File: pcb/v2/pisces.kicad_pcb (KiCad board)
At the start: 2 copper layers, 137.8 x 60.1 mm, 61 parts, among them J1 USB_B_Micro, J2 AudioJack4, SW1 SW_PUSH, SW10 SW_PUSH, SW11 SW_PUSH, SW12 SW_PUSH, SW13 SW_PUSH, SW14 SW_PUSH, SW15 SW_PUSH, SW16 SW_PUSH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

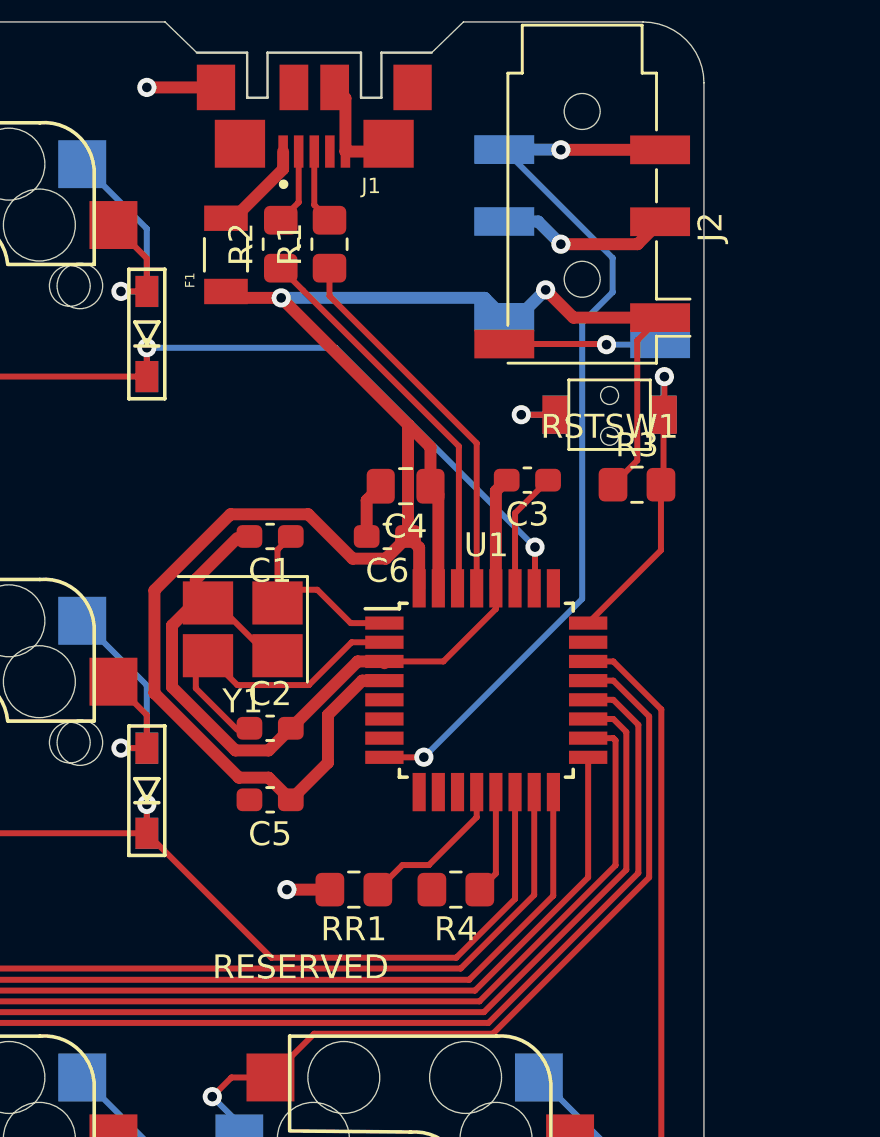
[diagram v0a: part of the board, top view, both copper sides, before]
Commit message: pisces V2.1 option 2 (SPLIT_HAND_MATRIX_GRID)
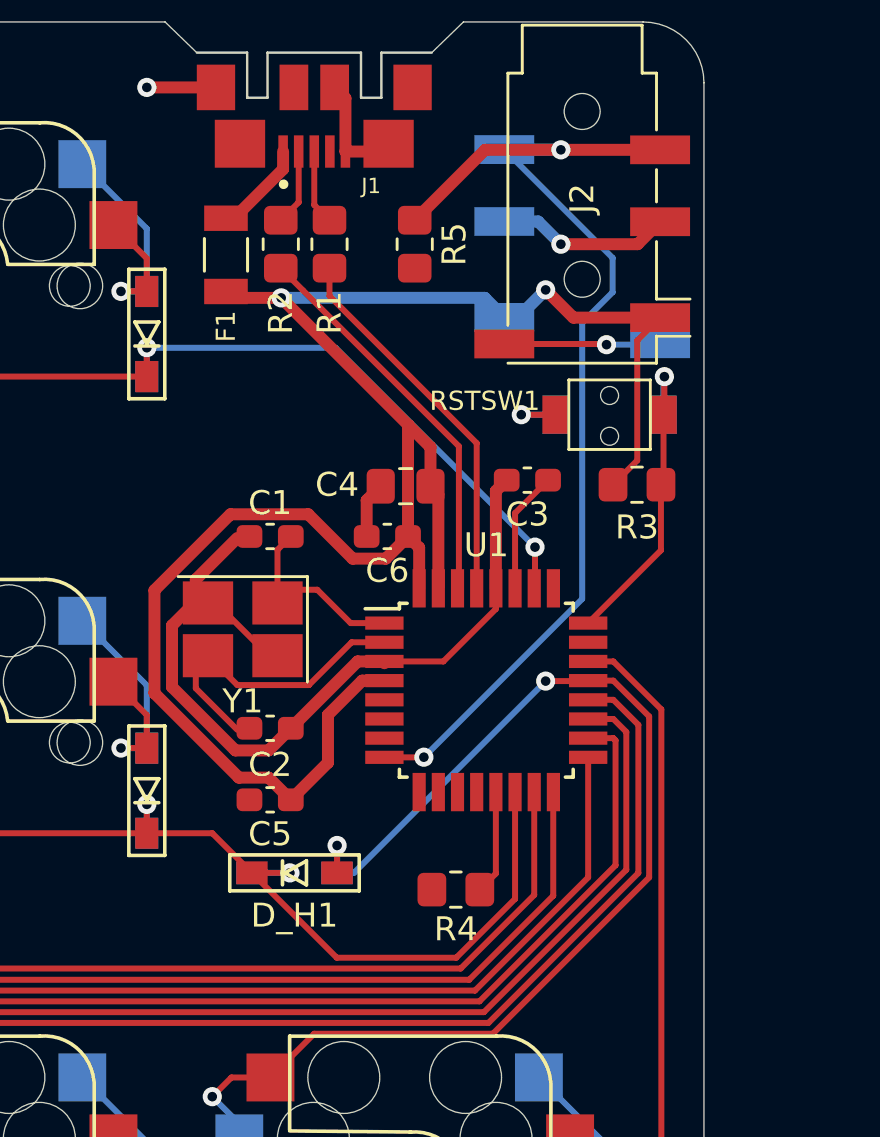
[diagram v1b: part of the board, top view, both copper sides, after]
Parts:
- removed RR1: 10k, Resistor_SMD:R_0805_2012Metric_Pad1.20x1.40mm_HandSolder
- added D_H1: D, kbd:D3_SMD, F.Cu at (159.7, 74.5)
- added R5: 10k, Resistor_SMD:R_0805_2012Metric_Pad1.20x1.40mm_HandSolder, F.Cu at (164.7, 48.3)
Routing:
- net col6: track 34.1 -> 50.2 mm, vias 1 -> 3
- net data: track 38.6 -> 45.9 mm
- net Net-(U1-Pad12): track 6.42 -> 0.00 mm
- net row1: track 132.7 -> 135.8 mm, vias 6 -> 7
- net GND: track 57.4 -> 55.6 mm, vias 4 -> 3
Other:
- board text added: "D_H1"
- board text added: "J2"
- board text added: "RSTSW1"
- board text added: "pisces v2.1 by knaruo"
- board text removed: "RESERVED"
- board text removed: "pisces v2.0 by knaruo"

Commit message: Updated KiCad version to 8.0, Supported JLCPCB PCBA info
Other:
- net class Default removed

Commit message: Revert "Updated KiCad version to 8.0, Supported JLCPCB PCBA info (#27)"
This reverts commit 94e640e821e110d7bb05b34c9f22027f3d2cd6e9.
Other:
- net class Default added: clearance 0.2, trace_width 0.25, via_dia 0.8, via_drill 0.4

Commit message: Removed R5 (resistor) from schematic (#30)
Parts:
- removed R5: 10k, Resistor_SMD:R_0805_2012Metric_Pad1.20x1.40mm_HandSolder
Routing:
- net data: track 45.9 -> 38.6 mm

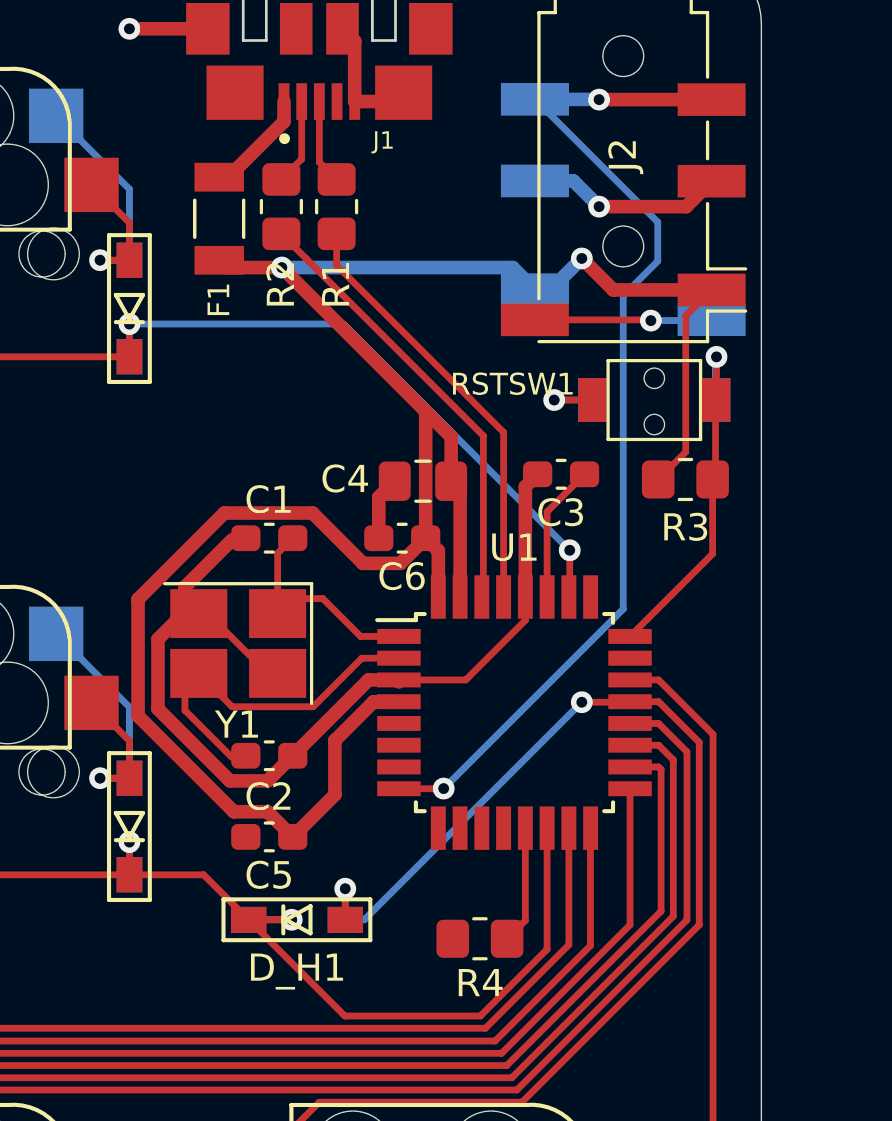
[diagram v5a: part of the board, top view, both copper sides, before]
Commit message: Stopped using hand-soldering footprint for most of parts
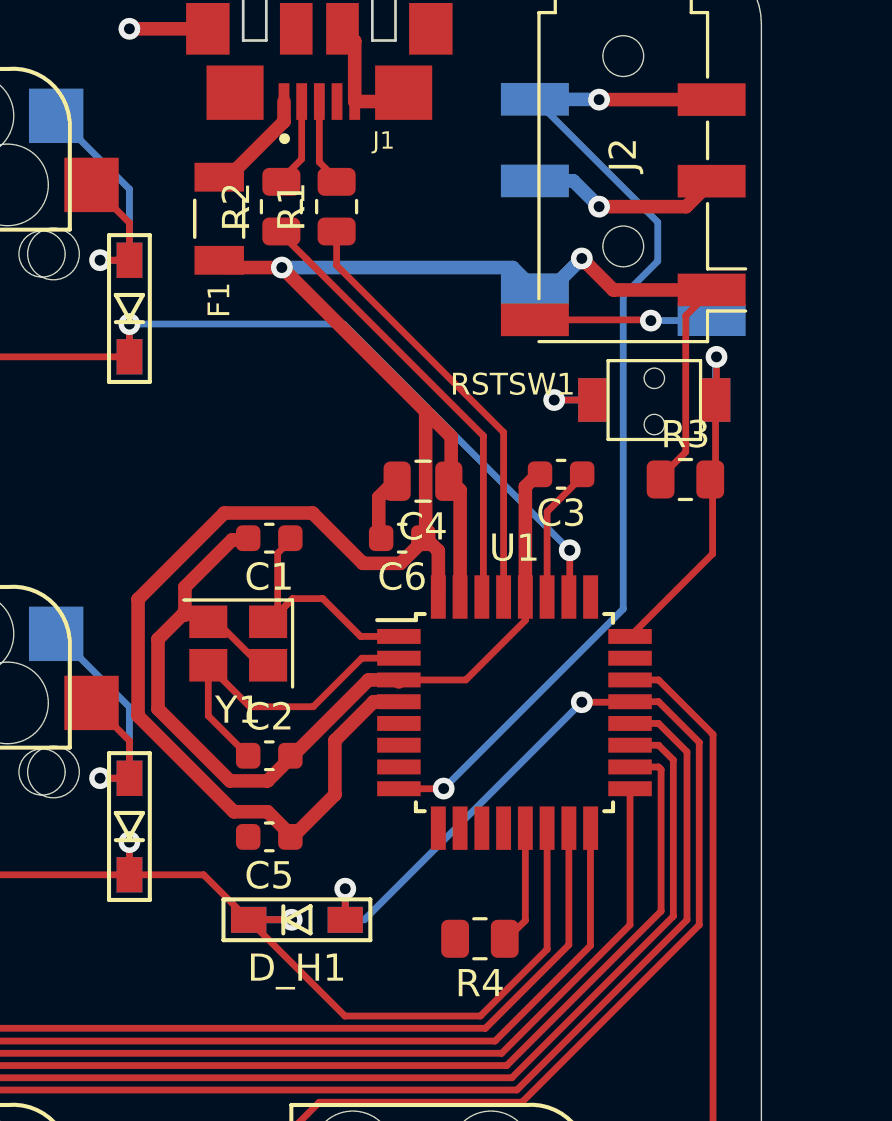
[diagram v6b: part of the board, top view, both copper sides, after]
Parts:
- C1, C2, C3, C5, C6: footprint Capacitor_SMD:C_0603_1608Metric_Pad1.08x0.95mm_HandSolder -> Capacitor_SMD:C_0603_1608Metric
- C4: footprint Capacitor_SMD:C_0805_2012Metric_Pad1.18x1.45mm_HandSolder -> Capacitor_SMD:C_0805_2012Metric
- R1, R2, R3, R4: footprint Resistor_SMD:R_0805_2012Metric_Pad1.20x1.40mm_HandSolder -> Resistor_SMD:R_0805_2012Metric
- Y1: footprint Crystal:Crystal_SMD_SeikoEpson_FA238-4Pin_3.2x2.5mm_HandSoldering -> Crystal:Crystal_SMD_SeikoEpson_FA238-4Pin_3.2x2.5mm

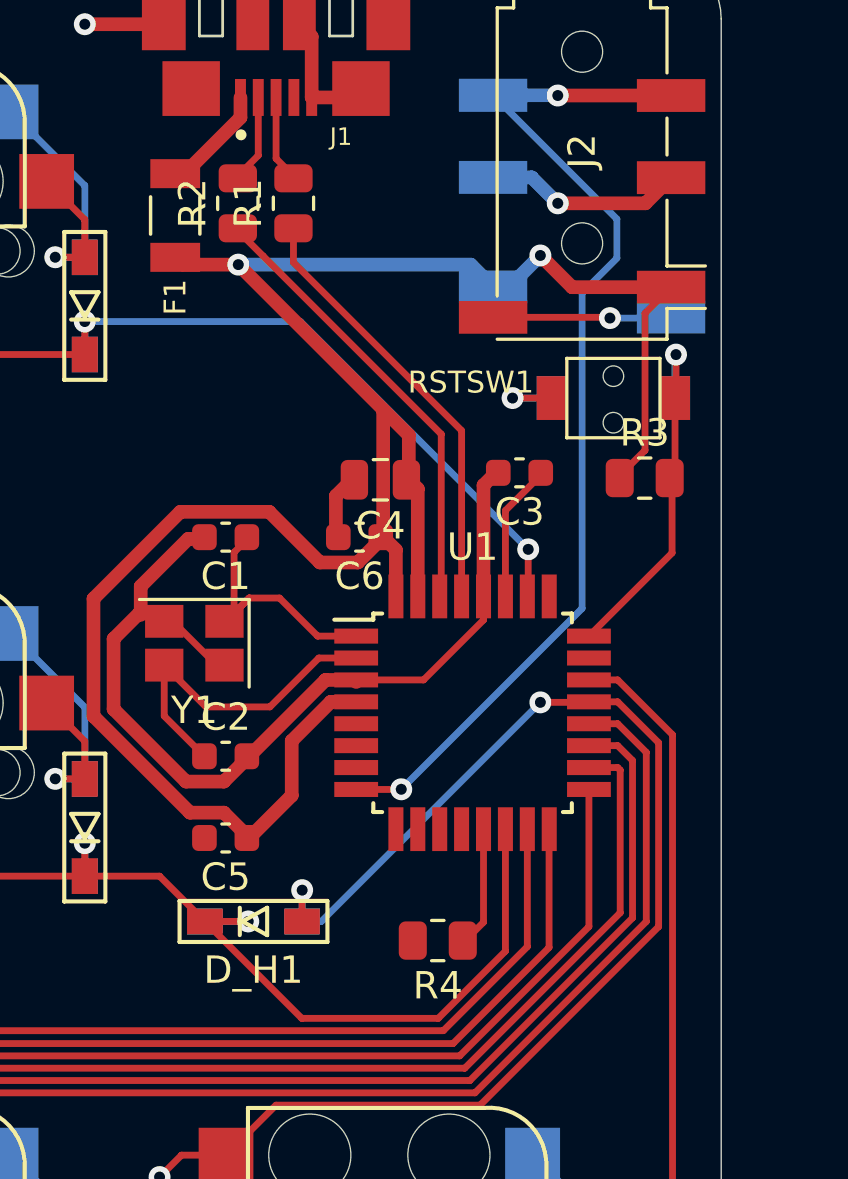
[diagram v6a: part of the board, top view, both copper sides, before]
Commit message: Resistors: 0805 --> 0603, Capacitors (other than 10u): 0603
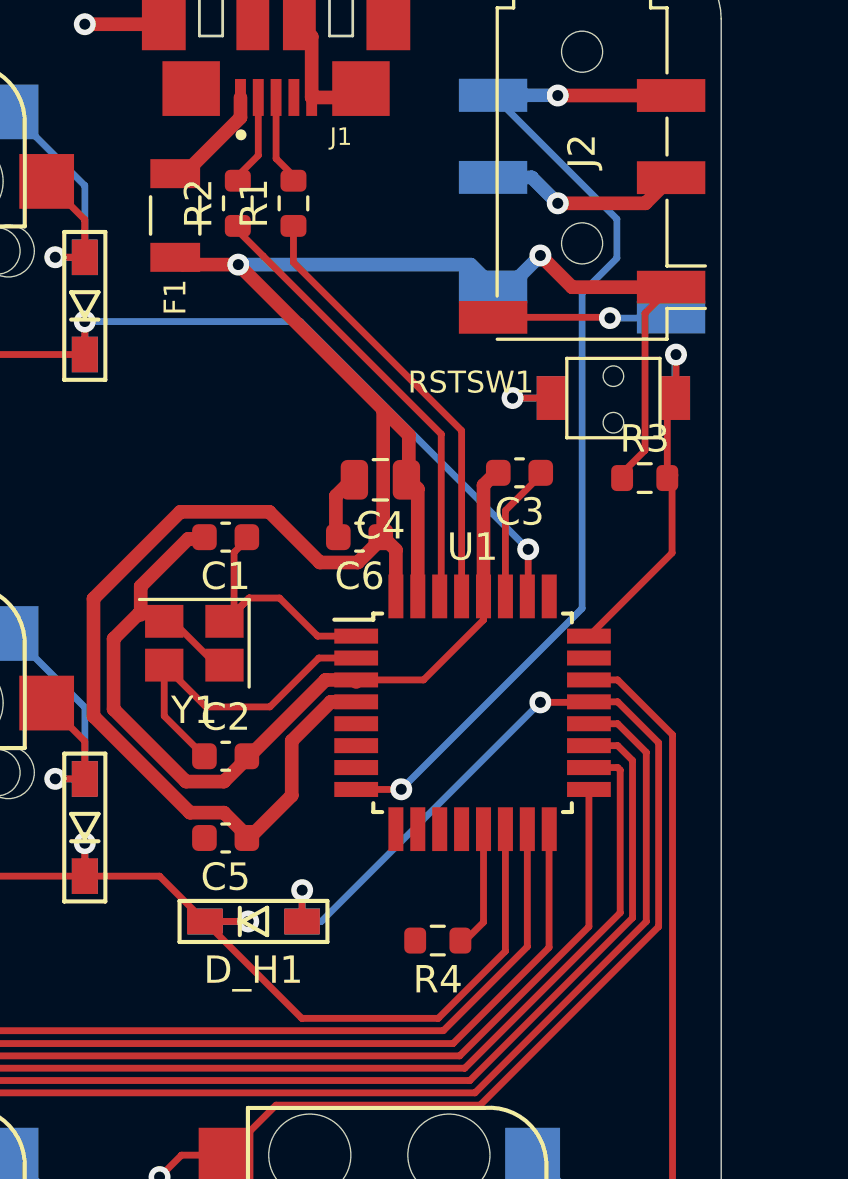
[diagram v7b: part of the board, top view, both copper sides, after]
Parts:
- R1, R2, R3, R4: footprint Resistor_SMD:R_0805_2012Metric -> Resistor_SMD:R_0603_1608Metric

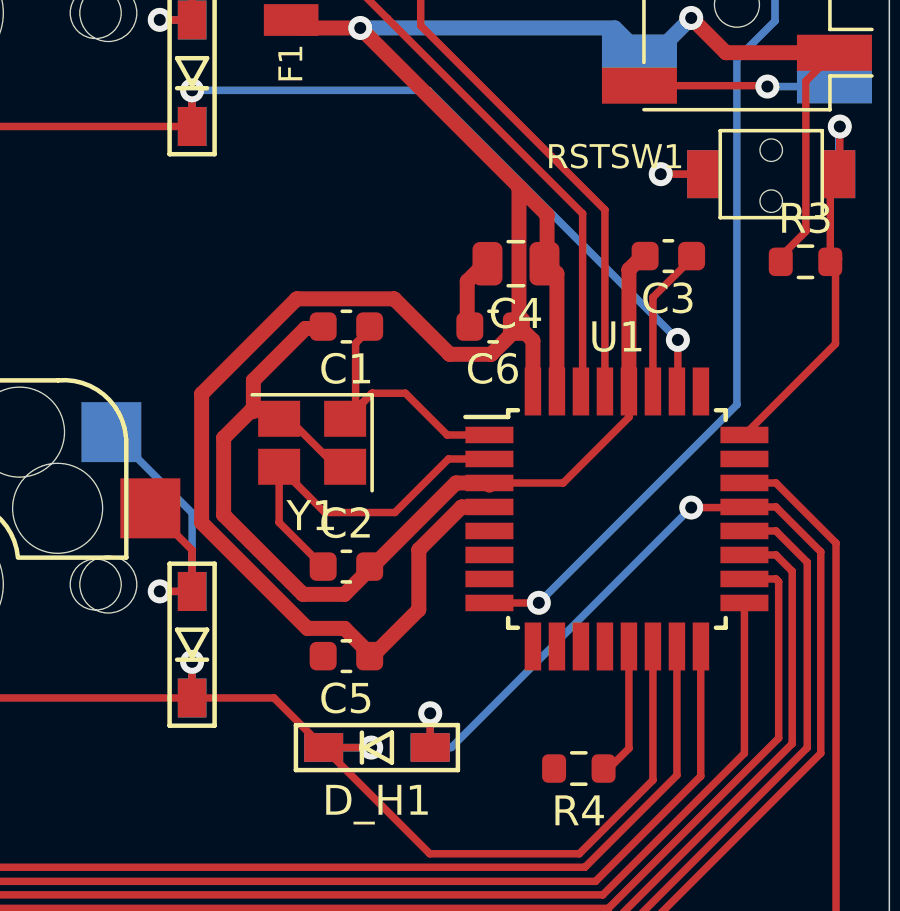
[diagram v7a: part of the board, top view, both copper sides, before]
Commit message: Smaller parts footprint
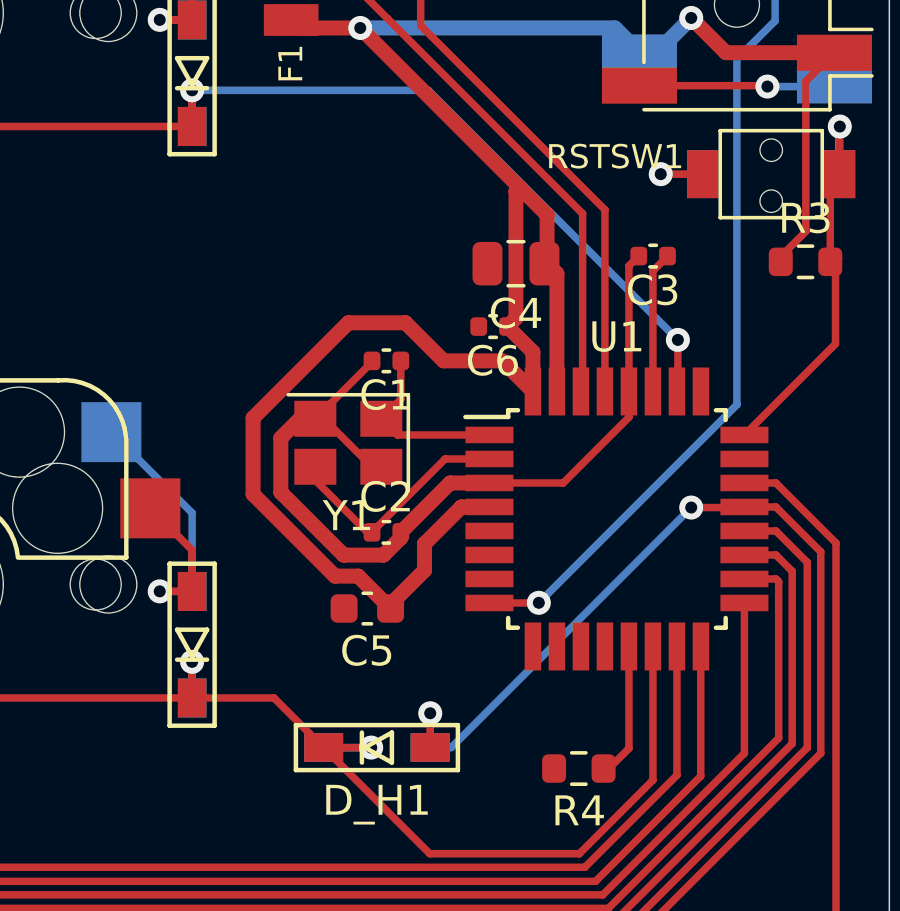
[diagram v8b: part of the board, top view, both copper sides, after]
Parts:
- C1, C2, C3, C6: footprint Capacitor_SMD:C_0603_1608Metric -> Capacitor_SMD:C_0402_1005Metric
- moved C1 1.76 mm to (160.0, 61.6)
- moved C2 1.76 mm to (160.0, 67.3)
- moved C5 1.73 mm to (159.4, 69.8)
- moved Y1 1.21 mm to (158.8, 64.3)
- moved C3 0.51 mm to (168.9, 58.1)
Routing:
- net GND: track 55.2 -> 47.2 mm
- net VCC: track 81.3 -> 75.2 mm
- net Net-(C2-Pad1): track 12.4 -> 7.99 mm
- net Net-(C1-Pad1): track 9.05 -> 6.03 mm
